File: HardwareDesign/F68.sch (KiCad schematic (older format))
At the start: 2 parts, among them J001 Conn_02x40_Counter_Clockwise

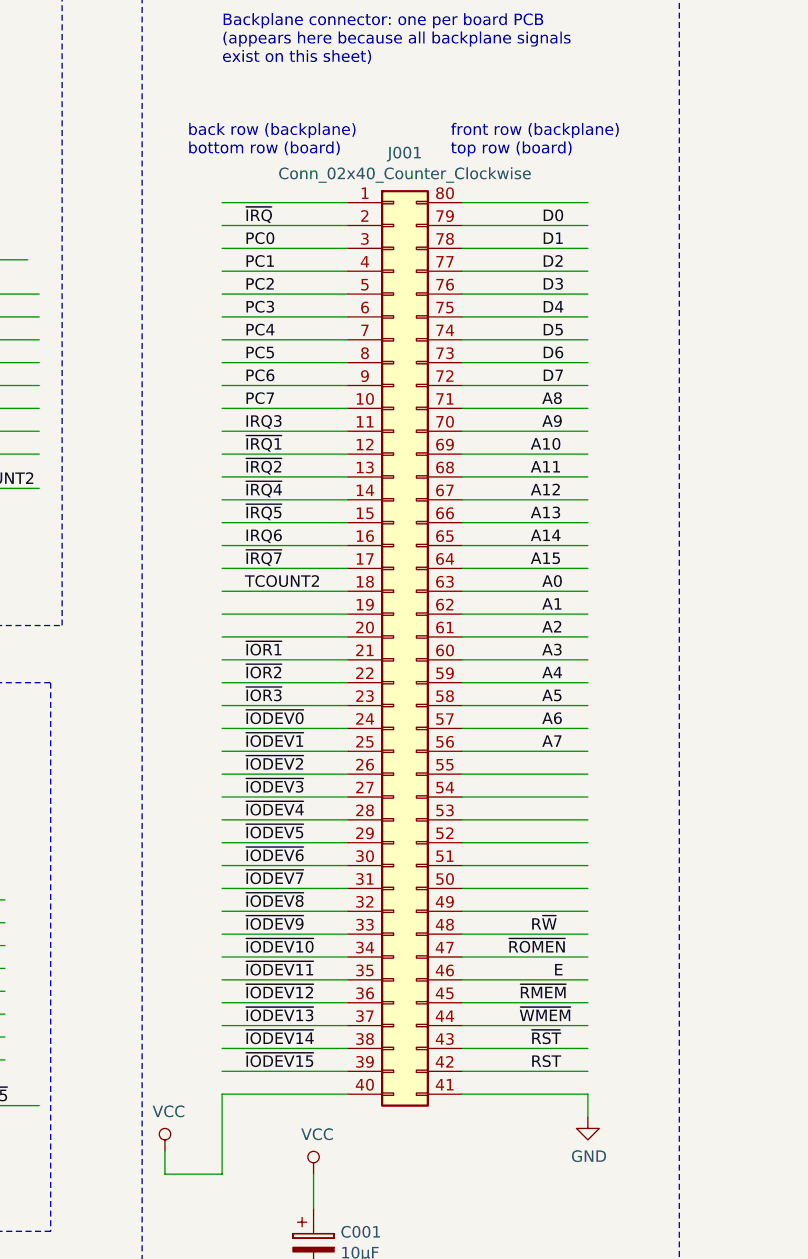
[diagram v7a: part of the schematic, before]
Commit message: fix pin assignments for backplane connector
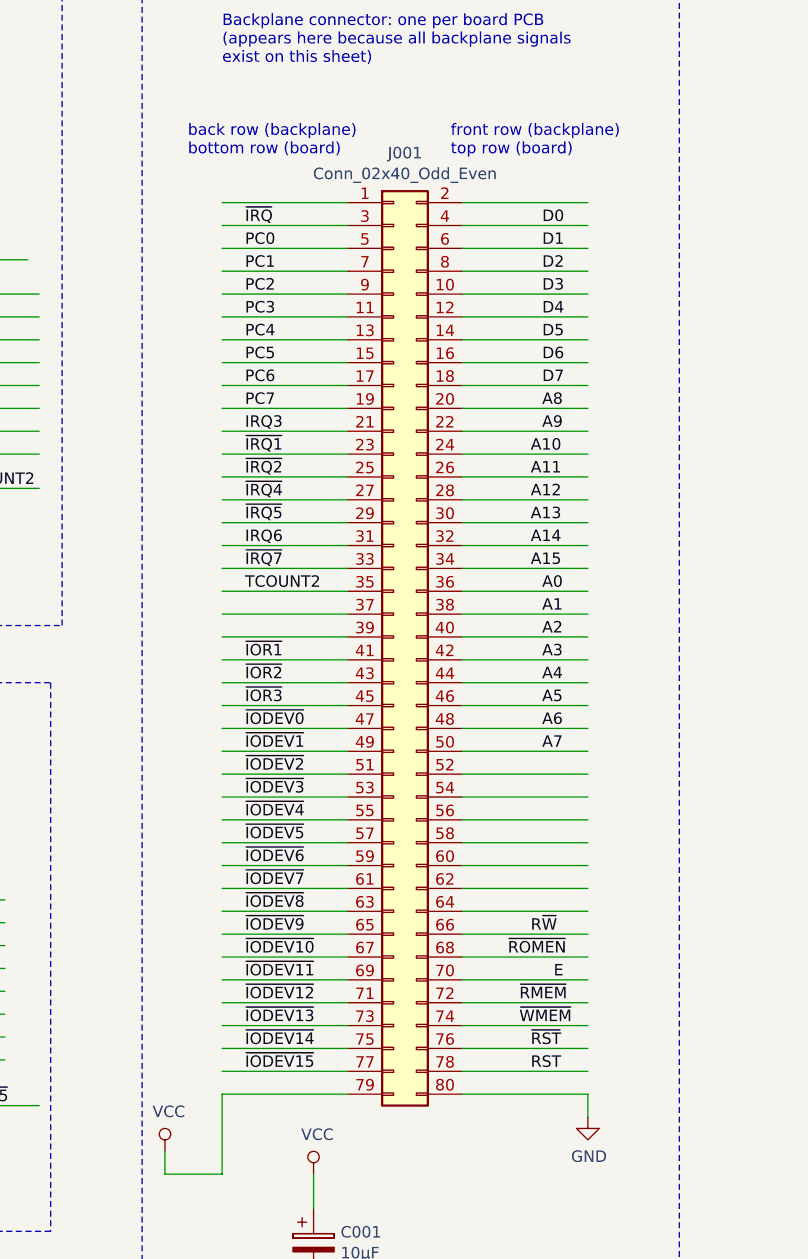
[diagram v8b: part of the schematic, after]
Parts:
- removed J001: Conn_02x40_Counter_Clockwise, Connector_PinHeader_2.54mm:PinHeader_2x40_P2.54mm_Vertical, symbol Connector_Generic:Conn_02x40_Counter_Clockwise
- added J001: Conn_02x40_Odd_Even, Connector_PinHeader_2.54mm:PinHeader_2x40_P2.54mm_Vertical, symbol Connector_Generic:Conn_02x40_Odd_Even
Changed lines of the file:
@@
 Text Label 7750 3650 0    50   ~ 0
 TCOUNT2
-$Comp
-L Connector_Generic:Conn_02x40_Counter_Clockwise J?
-U 1 1 6118356F
-P 9650 4300
-AR Path="/5CFA6AAA/6118356F" Ref="J?"  Part="1"
-AR Path="/5D49B078/6118356F" Ref="J?"  Part="1"
-AR Path="/6118356F" Ref="J001"  Part="1"
-F 0 "J001" H 9700 6417 50  0000 C CNN
-F 1 "Conn_02x40_Counter_Clockwise" H 9700 6326 50  0000 C CNN
-F 2 "Connector_PinHeader_2.54mm:PinHeader_2x40_P2.54mm_Vertical" H 9650 4300 50  0001 C CNN
-F 3 "~" H 9650 4300 50  0001 C CNN
-	1    9650 4300
-	1    0    0    -1
-$EndComp
 Wire Wire Line
 	8900 2400 9450 2400
@@
 Text Label 4500 6250 0    50   ~ 0
 ~IRQ7~
+$Comp
+L Connector_Generic:Conn_02x40_Odd_Even J001
+U 1 1 610D736D
+P 9650 4300
+F 0 "J001" H 9700 6417 50  0000 C CNN
+F 1 "Conn_02x40_Odd_Even" H 9700 6326 50  0000 C CNN
+F 2 "Connector_PinHeader_2.54mm:PinHeader_2x40_P2.54mm_Vertical" H 9650 4300 50  0001 C CNN
+F 3 "~" H 9650 4300 50  0001 C CNN
+	1    9650 4300
+	1    0    0    -1
+$EndComp
 $EndSCHEMATC
